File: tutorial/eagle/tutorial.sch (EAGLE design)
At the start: 16 parts, among them X2 8MHz, X4 MINI-USB

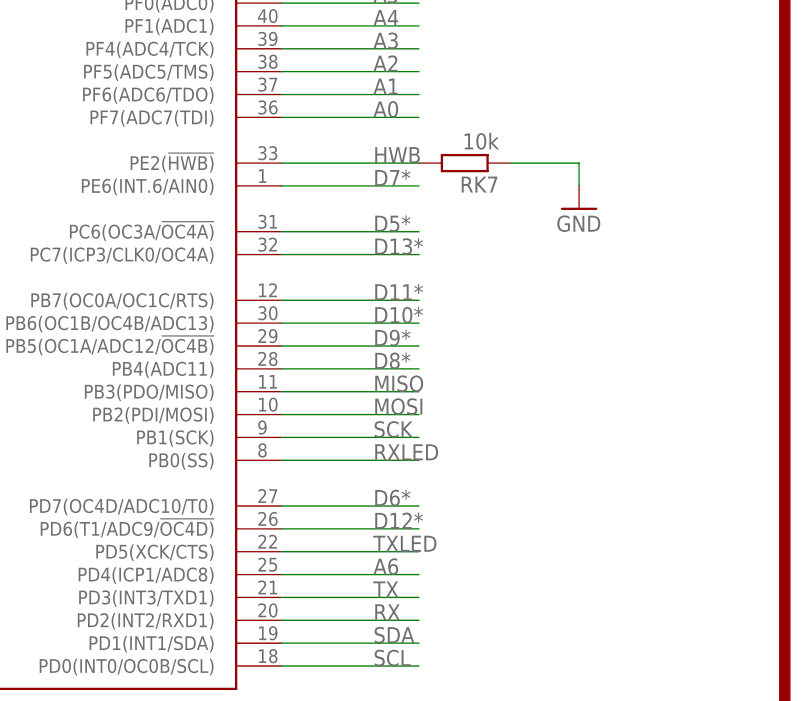
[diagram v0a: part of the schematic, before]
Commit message: rename pins in tutorial
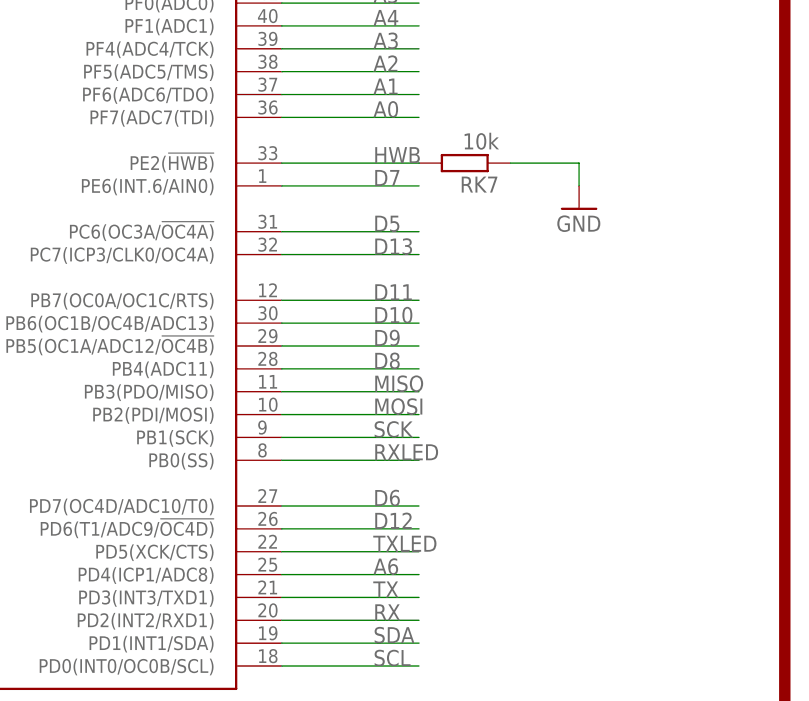
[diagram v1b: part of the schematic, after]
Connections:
- net D10* renamed D10
- net D11* renamed D11
- net D12* renamed D12
- net D13* renamed D13
- net D5* renamed D5
- net D6* renamed D6
- net D7* renamed D7
- net D8* renamed D8
- net D9* renamed D9
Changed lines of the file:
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@@
 <?xml version="1.0" encoding="utf-8"?>
 <!DOCTYPE eagle SYSTEM "eagle.dtd">
-<eagle version="8.3.2">
+<eagle version="8.5.0">
 <drawing>
 <settings>
-<setting alwaysvectorfont="yes"/>
+<setting alwaysvectorfont="no"/>
 <setting keepoldvectorfont="yes"/>
 <setting verticaltext="up"/>
@@
 </segment>
 </net>
-<net name="D11*" class="0">
+<net name="D11" class="0">
 <segment>
 <pinref part="32U4" gate="G$1" pin="PB7(OC0A/OC1C/RTS)"/>
@@
 </segment>
 </net>
-<net name="D9*" class="0">
+<net name="D9" class="0">
 <segment>
 <pinref part="32U4" gate="G$1" pin="PB5(OC1A/ADC12/!OC4B)"/>
@@
 </segment>
 </net>
-<net name="D5*" class="0">
+<net name="D5" class="0">
 <segment>
 <pinref part="32U4" gate="G$1" pin="PC6(OC3A/!OC4A)"/>
@@
 </segment>
 </net>
-<net name="D6*" class="0">
+<net name="D6" class="0">
 <segment>
 <pinref part="32U4" gate="G$1" pin="PD7(OC4D/ADC10/T0)"/>
@@
 </segment>
 </net>
-<net name="D10*" class="0">
+<net name="D10" class="0">
 <segment>
 <pinref part="32U4" gate="G$1" pin="PB6(OC1B/OC4B/ADC13)"/>
@@
 </segment>
 </net>
-<net name="D7*" class="0">
+<net name="D7" class="0">
 <segment>
 <pinref part="32U4" gate="G$1" pin="PE6(INT.6/AIN0)"/>
@@
 </segment>
 </net>
-<net name="D13*" class="0">
+<net name="D13" class="0">
 <segment>
 <pinref part="32U4" gate="G$1" pin="PC7(ICP3/CLK0/OC4A)"/>
@@
 </segment>
 </net>
-<net name="D12*" class="0">
+<net name="D12" class="0">
 <segment>
 <pinref part="32U4" gate="G$1" pin="PD6(T1/ADC9/!OC4D)"/>
@@
 </segment>
 </net>
-<net name="D8*" class="0">
+<net name="D8" class="0">
 <segment>
 <pinref part="32U4" gate="G$1" pin="PB4(ADC11)"/>

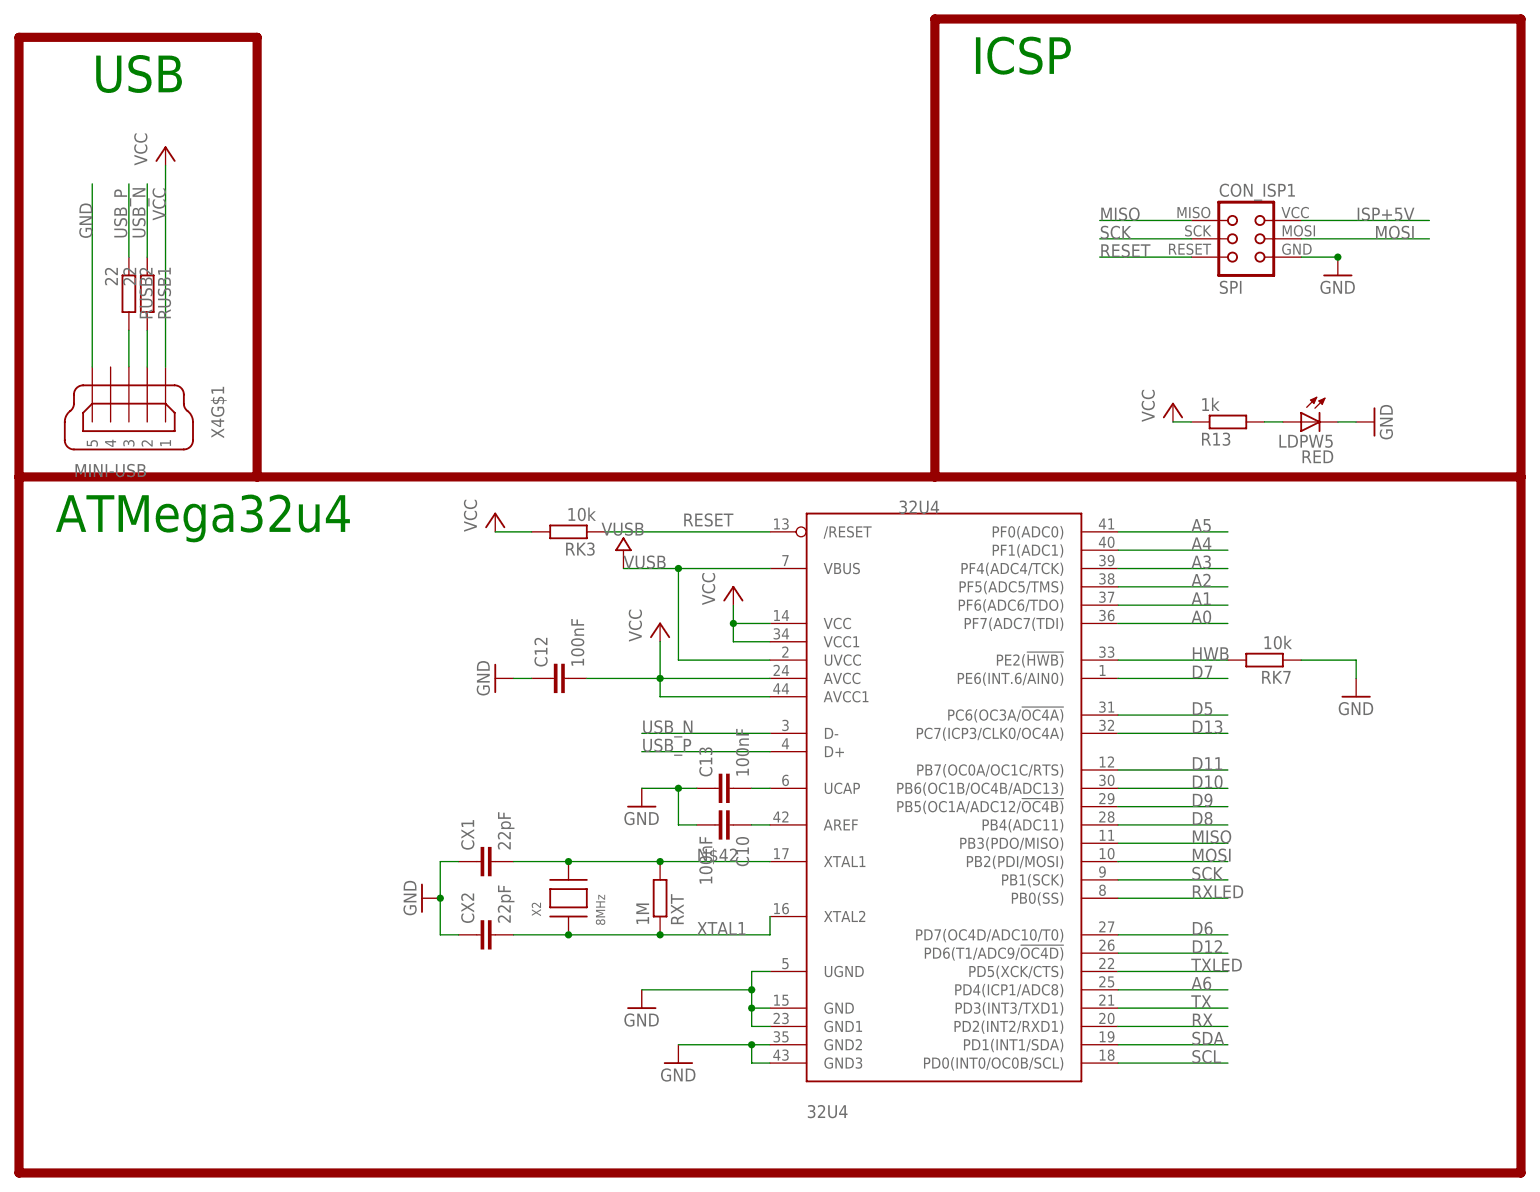
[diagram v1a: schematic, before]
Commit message: update part name
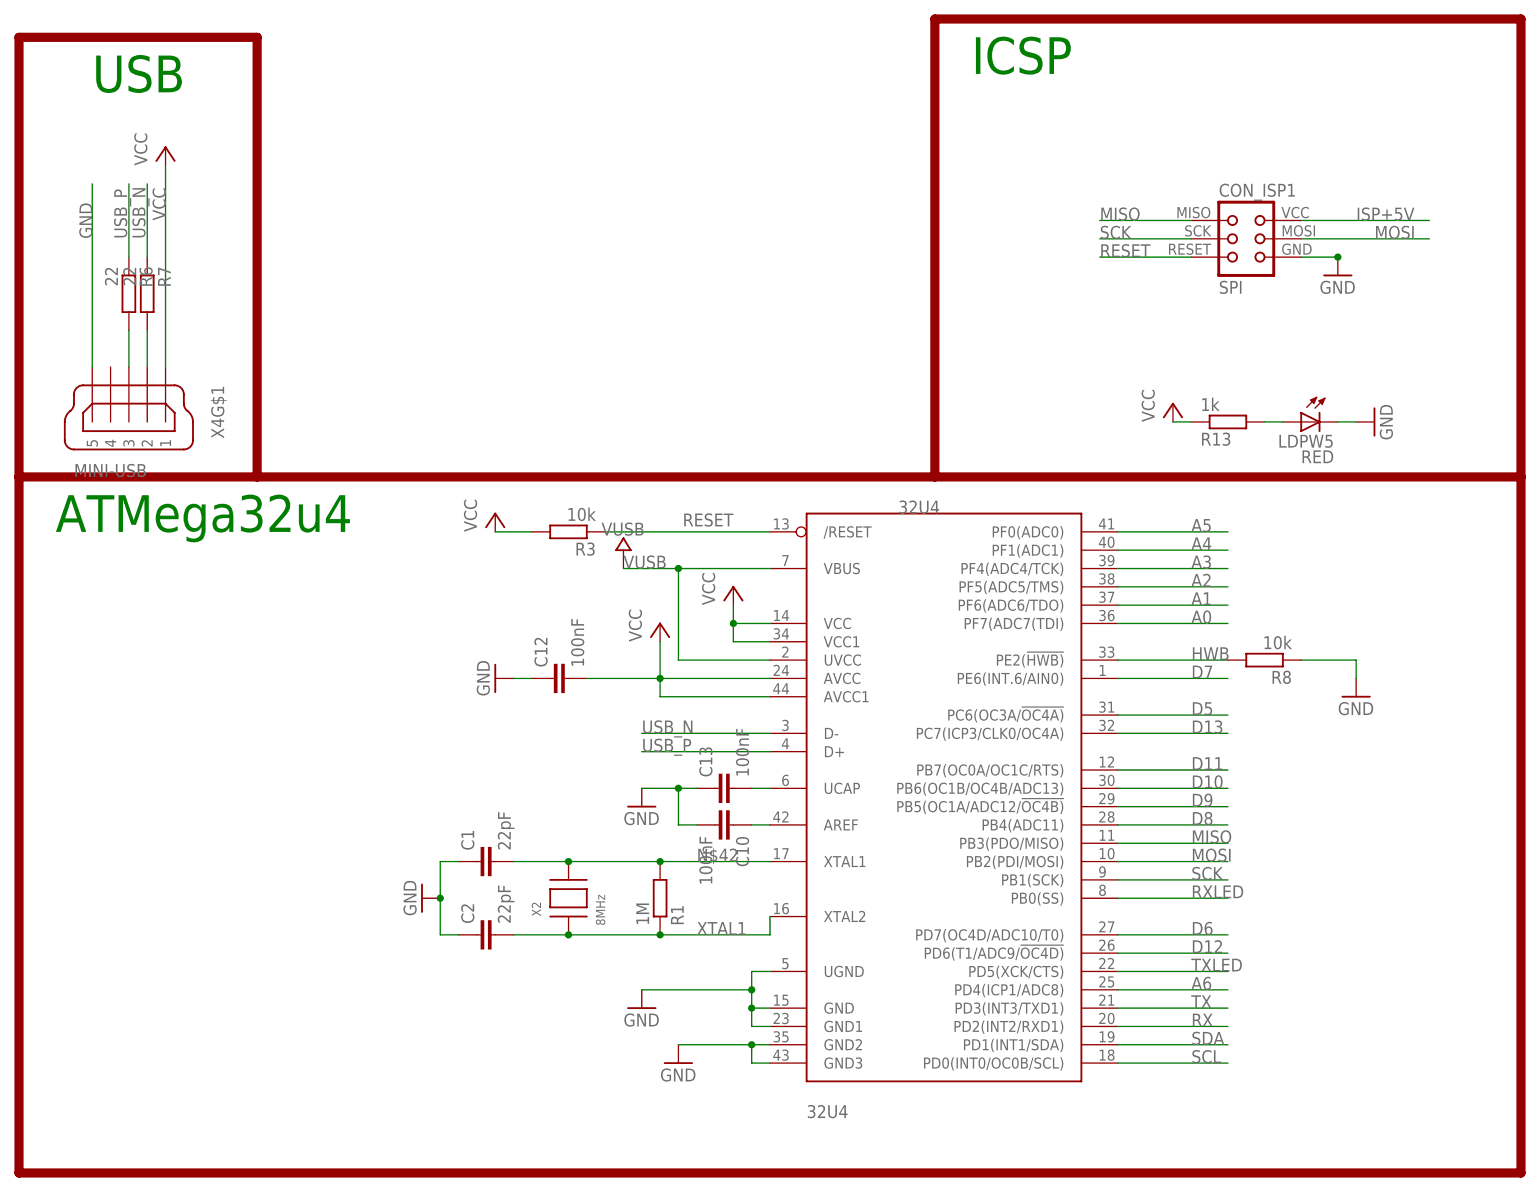
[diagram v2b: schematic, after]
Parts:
- renumbered CX1 to C1, CX2 to C2, RK3 to R3, RK7 to R8, RUSB1 to R7, RUSB2 to R6, RXT to R1

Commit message: update gerber to v1.6.1
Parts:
- added LED1, LED2, LED3: (no value), led:LED5MM
- added R2, R4, R5: (no value), rcl:R-EU_R1206
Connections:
- new net N$5: LED3.C, R5.1
- new net N$6: LED2.C, R4.1
- new net N$7: LED1.C, R2.2
- net A0: now also LED1.A
- net A1: now also LED2.A
- net A2: now also LED3.A
- net GND: now also R2.1, R4.2, R5.2
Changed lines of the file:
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@@
 <?xml version="1.0" encoding="utf-8"?>
 <!DOCTYPE eagle SYSTEM "eagle.dtd">
-<eagle version="8.6.0">
+<eagle version="8.7.0">
 <drawing>
 <settings>
@@
 <part name="CON_ISP1" library="lpatiny" deviceset="TINYISP" device="" value="SPI"/>
 <part name="GND11" library="supply1" library_urn="urn:adsk.eagle:library:371" deviceset="GND" device=""/>
+<part name="LED1" library="led" library_urn="urn:adsk.eagle:library:259" deviceset="LED" device="5MM" package3d_urn="urn:adsk.eagle:package:15799/2"/>
+<part name="LED2" library="led" library_urn="urn:adsk.eagle:library:259" deviceset="LED" device="5MM" package3d_urn="urn:adsk.eagle:package:15799/2"/>
+<part name="LED3" library="led" library_urn="urn:adsk.eagle:library:259" deviceset="LED" device="5MM" package3d_urn="urn:adsk.eagle:package:15799/2"/>
+<part name="R2" library="rcl" library_urn="urn:adsk.eagle:library:334" deviceset="R-EU_" device="R1206" package3d_urn="urn:adsk.eagle:package:23540/2">
+<spice>
+<pinmapping spiceprefix="R">
+<pinmap gate="G$1" pin="1" pinorder="1"/>
+<pinmap gate="G$1" pin="2" pinorder="2"/>
+</pinmapping>
+</spice>
+<attribute name="LCSC" value="12345"/>
+</part>
+<part name="R4" library="rcl" library_urn="urn:adsk.eagle:library:334" deviceset="R-EU_" device="R1206" package3d_urn="urn:adsk.eagle:package:23540/2"/>
+<part name="R5" library="rcl" library_urn="urn:adsk.eagle:library:334" deviceset="R-EU_" device="R1206" package3d_urn="urn:adsk.eagle:package:23540/2"/>
+<part name="GND1" library="supply1" library_urn="urn:adsk.eagle:library:371" deviceset="GND" device=""/>
 </parts>
 <sheets>
@@
 <instance part="CON_ISP1" gate="G$1" x="154.94" y="259.08"/>
 <instance part="GND11" gate="1" x="167.64" y="254"/>
+<instance part="LED1" gate="G$1" x="50.8" y="274.32" rot="R90"/>
+<instance part="LED2" gate="G$1" x="50.8" y="261.62" rot="R90"/>
+<instance part="LED3" gate="G$1" x="50.8" y="248.92" rot="R90"/>
+<instance part="R2" gate="G$1" x="71.12" y="274.32" rot="R180">
+<attribute name="LCSC" x="71.12" y="274.32" size="1.778" layer="96" rot="R180" display="off"/>
+</instance>
+<instance part="R4" gate="G$1" x="71.12" y="261.62"/>
+<instance part="R5" gate="G$1" x="71.12" y="248.92"/>
+<instance part="GND1" gate="1" x="86.36" y="241.3"/>
 </instances>
 <busses>
@@
 <junction x="167.64" y="256.54"/>
 </segment>
+<segment>
+<pinref part="R2" gate="G$1" pin="1"/>
+<wire x1="76.2" y1="274.32" x2="86.36" y2="274.32" width="0.1524" layer="91"/>
+<wire x1="86.36" y1="274.32" x2="86.36" y2="261.62" width="0.1524" layer="91"/>
+<pinref part="R4" gate="G$1" pin="2"/>
+<wire x1="86.36" y1="261.62" x2="86.36" y2="248.92" width="0.1524" layer="91"/>
+<wire x1="86.36" y1="248.92" x2="86.36" y2="243.84" width="0.1524" layer="91"/>
+<wire x1="76.2" y1="261.62" x2="86.36" y2="261.62" width="0.1524" layer="91"/>
+<junction x="86.36" y="261.62"/>
+<pinref part="R5" gate="G$1" pin="2"/>
+<wire x1="76.2" y1="248.92" x2="86.36" y2="248.92" width="0.1524" layer="91"/>
+<junction x="86.36" y="248.92"/>
+<pinref part="GND1" gate="1" pin="GND"/>
+</segment>
 </net>
 <net name="SCK" class="0">
@@
 <label x="147.32" y="210.82" size="1.778" layer="95"/>
 </segment>
+<segment>
+<pinref part="LED3" gate="G$1" pin="A"/>
+<wire x1="48.26" y1="248.92" x2="38.1" y2="248.92" width="0.1524" layer="91"/>
+<label x="38.1" y="248.92" size="1.778" layer="95"/>
+</segment>
 </net>
 <net name="A3" class="0">
@@
 <wire x1="137.16" y1="208.28" x2="152.4" y2="208.28" width="0.1524" layer="91"/>
 <label x="147.32" y="208.28" size="1.778" layer="95"/>
+</segment>
+<segment>
+<pinref part="LED2" gate="G$1" pin="A"/>
+<wire x1="48.26" y1="261.62" x2="38.1" y2="261.62" width="0.1524" layer="91"/>
+<label x="38.1" y="261.62" size="1.778" layer="95"/>
 </segment>
 </net>
@@
 <wire x1="137.16" y1="205.74" x2="152.4" y2="205.74" width="0.1524" layer="91"/>
 <label x="147.32" y="205.74" size="1.778" layer="95"/>
+</segment>
+<segment>
+<pinref part="LED1" gate="G$1" pin="A"/>
+<wire x1="48.26" y1="274.32" x2="38.1" y2="274.32" width="0.1524" layer="91"/>
+<label x="38.1" y="274.32" size="1.778" layer="95"/>
 </segment>
 </net>
@@
 </segment>
 </net>
+<net name="N$5" class="0">
+<segment>
+<pinref part="LED3" gate="G$1" pin="C"/>
+<pinref part="R5" gate="G$1" pin="1"/>
+<wire x1="55.88" y1="248.92" x2="66.04" y2="248.92" width="0.1524" layer="91"/>
+</segment>
+</net>
+<net name="N$6" class="0">
+<segment>
+<pinref part="LED2" gate="G$1" pin="C"/>
+<pinref part="R4" gate="G$1" pin="1"/>
+<wire x1="55.88" y1="261.62" x2="66.04" y2="261.62" width="0.1524" layer="91"/>
+</segment>
+</net>
+<net name="N$7" class="0">
+<segment>
+<pinref part="LED1" gate="G$1" pin="C"/>
+<pinref part="R2" gate="G$1" pin="2"/>
+<wire x1="55.88" y1="274.32" x2="66.04" y2="274.32" width="0.1524" layer="91"/>
+</segment>
+</net>
